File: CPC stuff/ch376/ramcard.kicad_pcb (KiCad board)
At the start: 2 copper layers, 69.1 x 40.4 mm, 30 parts, among them IC1 74LS20, IC2 74LS02, IC3 74LS138, IC4 CH376, P1 CONN_25X2, P2 USB_A, P3 USB_B, U1 LD1117S33CTR, U2 CONN_SD, U3 TL16C550C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

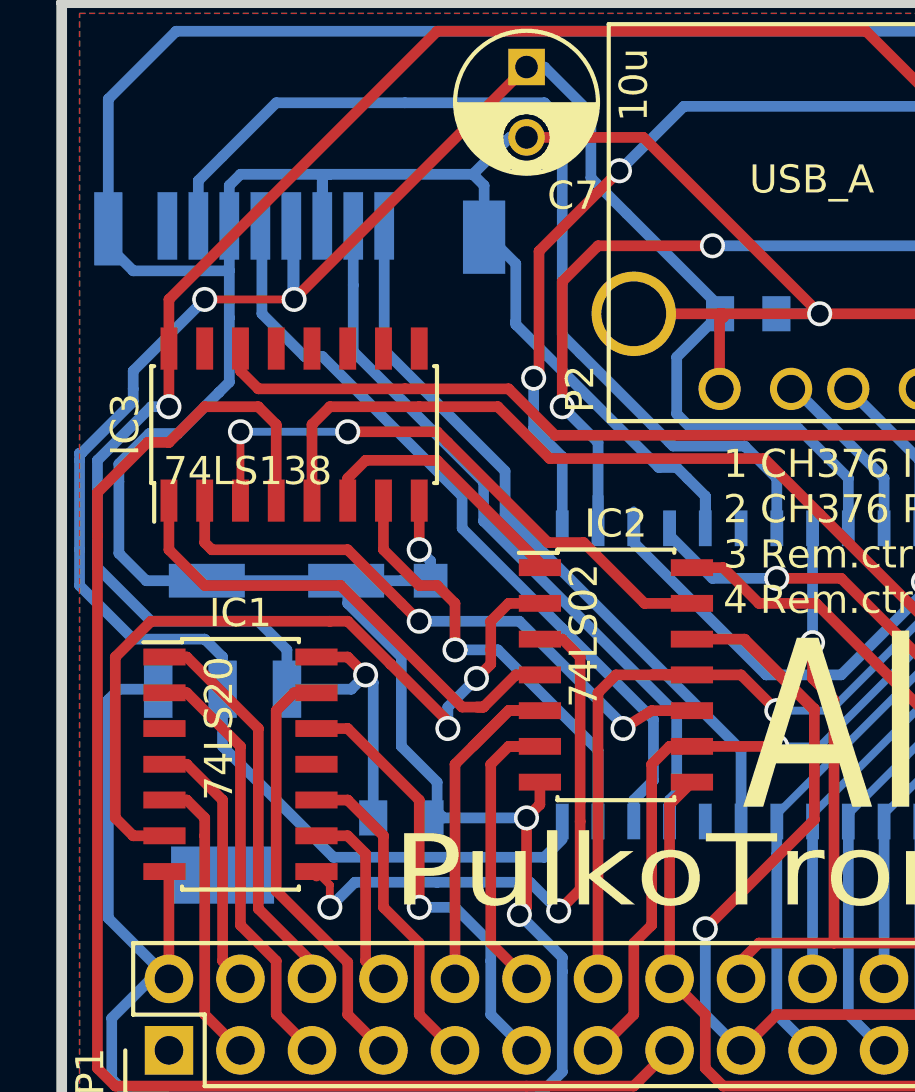
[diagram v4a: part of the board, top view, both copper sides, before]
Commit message: Fix SD card pinout.
git-svn-id: svn://pulkomandy.tk/avrstuff@121 c6672c3c-f6b6-47f9-9001-1fd6b12fecbe
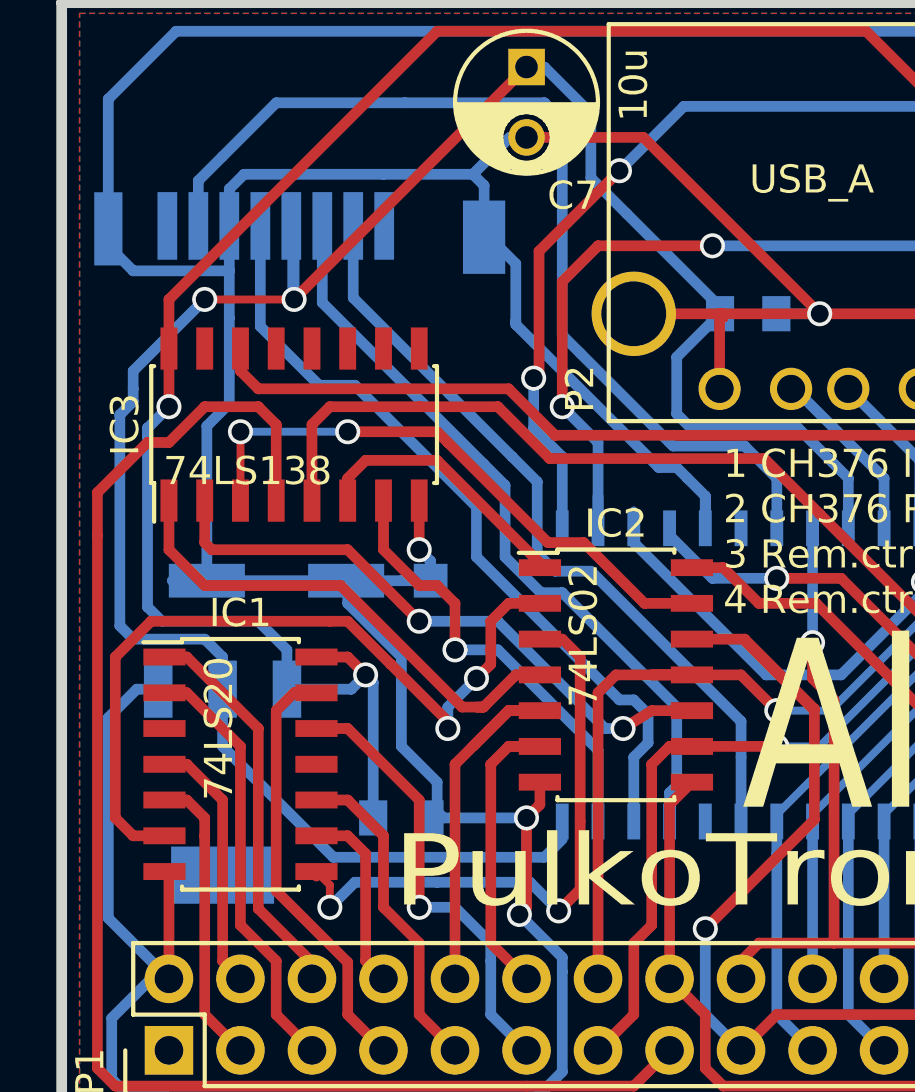
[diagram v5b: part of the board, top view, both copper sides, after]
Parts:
- U2: value CONN_SD -> CONN_microSD
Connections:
- U2 pad 1: //SD_CS -> (no net)
- U2 pad 2: /SD_DI -> //SD_CS
- U2 pad 3: GND -> /SD_DI
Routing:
- net GND: track 446.6 -> 438.3 mm
- net VCC: track 272.6 -> 271.1 mm
- net +3V3: track 80.5 -> 79.2 mm
- net //SD_CS: track 26.4 -> 27.6 mm
- net /SD_DI: track 26.0 -> 26.9 mm
- net /SD_CLK: track 27.6 -> 28.2 mm

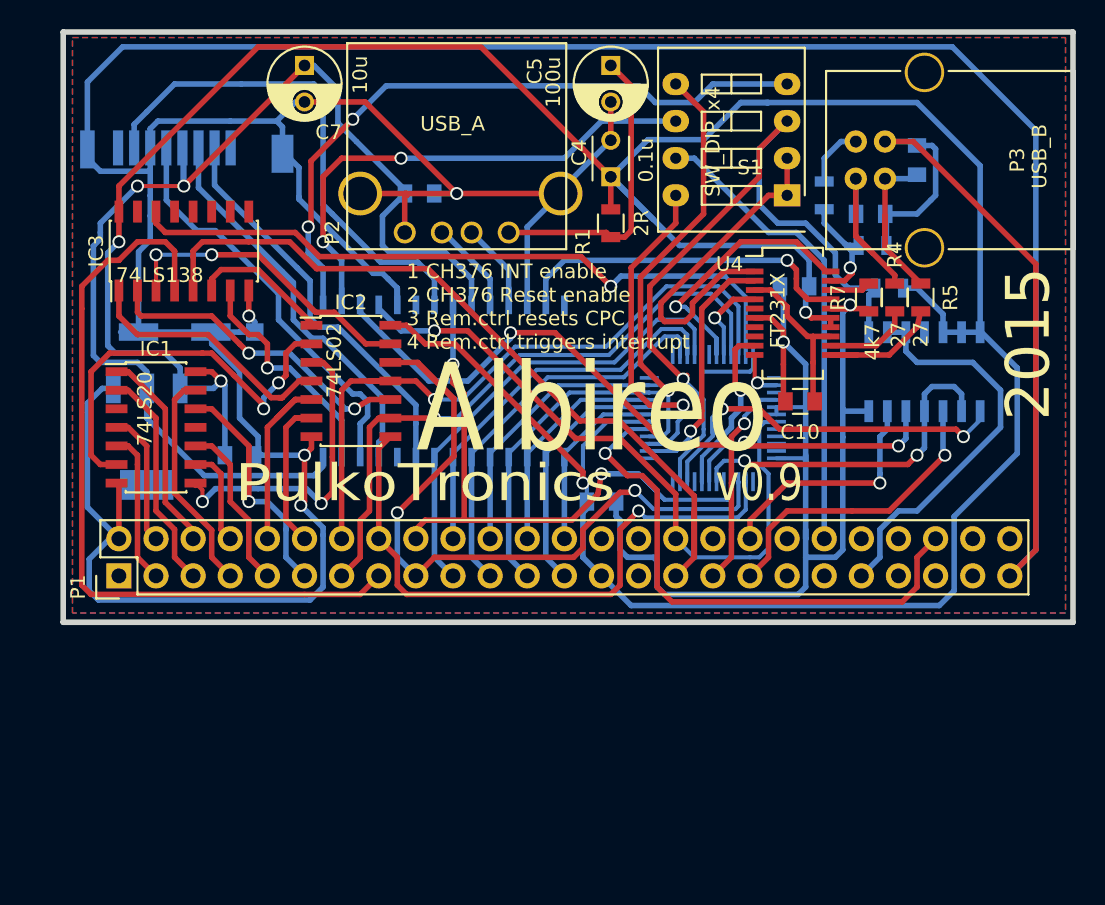
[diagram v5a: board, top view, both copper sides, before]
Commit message: Board version 1.0
- Add footprint for CH376 activity LED (not populated on my boards)
- Change version and year on silkscreen
- Minor routing fixes and improvements
- Add all capacitor values

git-svn-id: svn://pulkomandy.tk/avrstuff@122 c6672c3c-f6b6-47f9-9001-1fd6b12fecbe
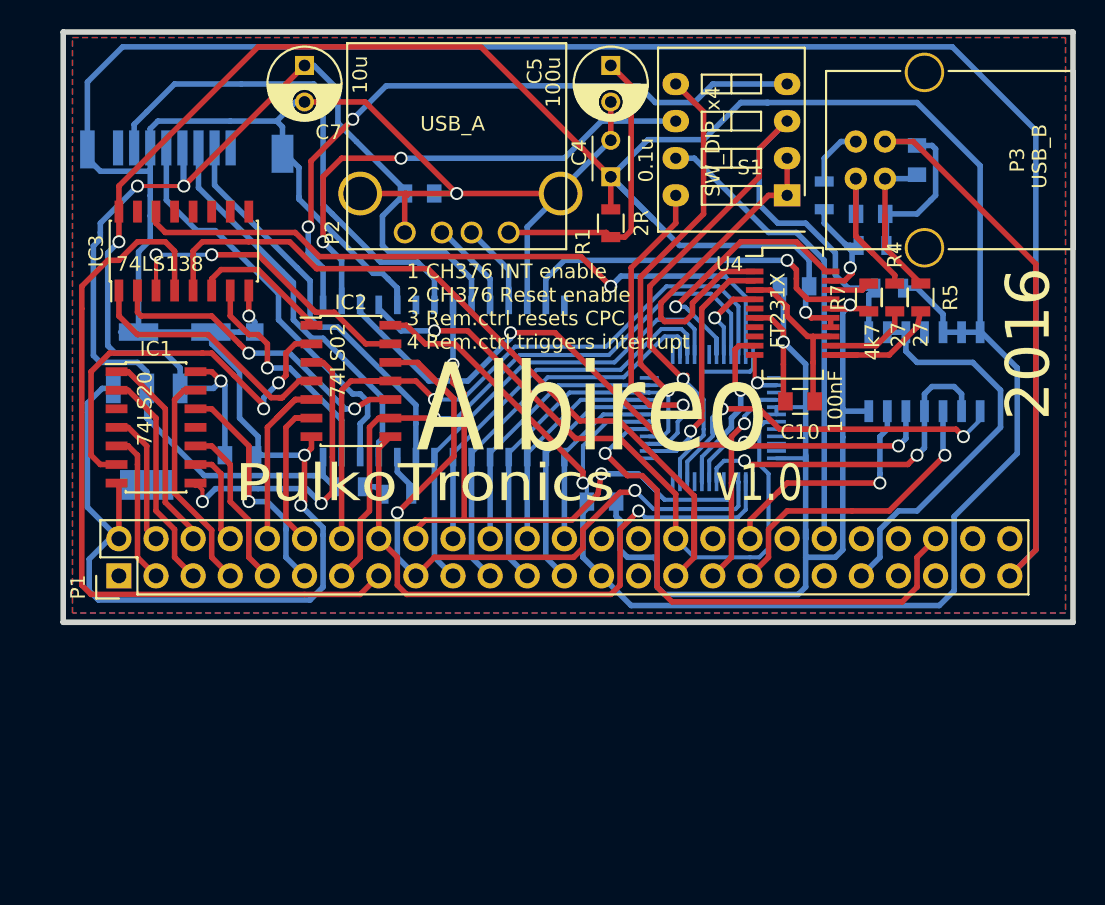
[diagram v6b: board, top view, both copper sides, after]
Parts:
- added D1: LED, Resistors_SMD:R_0805, B.Cu at (37.3, 61.2)
- added R8: 1K, Resistors_SMD:R_0805, B.Cu at (40.6, 61.7)
- C2, C3: value C -> 1uF
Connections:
- IC4 pad 24: (no net) -> Net-(IC4-Pad24)
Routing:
- net Net-(IC4-Pad24): track 0.00 -> 3.44 mm
- net +3V3: track 79.2 -> 81.4 mm
- net Net-(D1-Pad1): track 0.00 -> 1.61 mm
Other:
- board text added: "2016"
- board text added: "v1.0"
- board text removed: "2015"
- board text removed: "v0.9"
